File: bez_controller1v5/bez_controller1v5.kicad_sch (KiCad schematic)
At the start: 71 parts, among them J1 Conn_01x03_Male, J10 Barrel_Jack, J11 Conn_01x03_Male, J12 Conn_01x03_Male, J13 USB_B_Mini, J2 Conn_01x03_Male, J3 Conn_01x03_Male, J4 Conn_01x03_Male, J5 Conn_01x03_Male, J6 Conn_01x03_Male, J7 Conn_01x03_Male, J8 IMU Conn_01x08_Female, J9 JTAG Conn_01x06_Male, U1 74LVC2G241, U10 STM32F446RETx, U11 USBLC6-2SC6, U2 74LVC2G241, U3 74LVC2G241, U4 74LVC2G241, U5 74LVC2G241, U6 74LVC2G241, U7 PX07806-500-S, U8 LF50ABV_TO220, U9 LD1117AS33TR_SOT223, Y1 8MHz

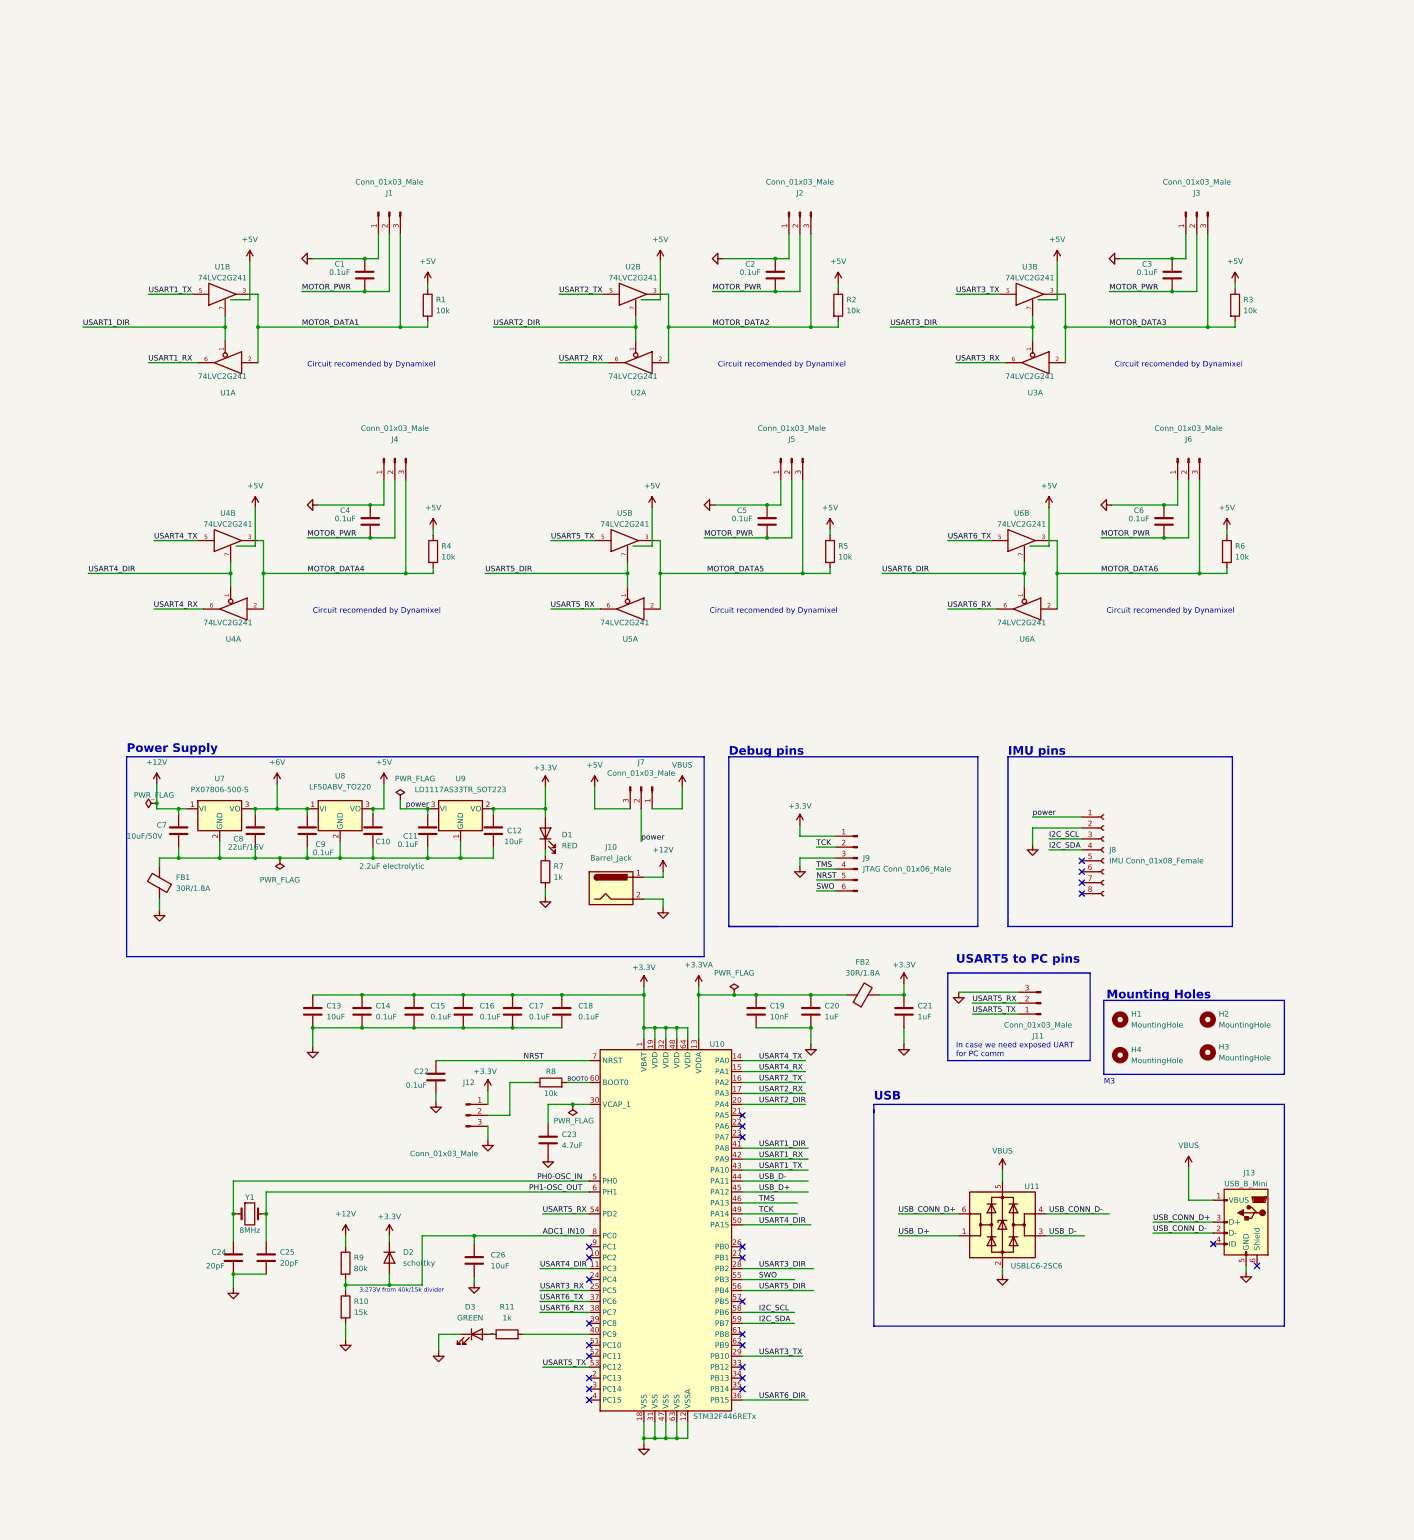
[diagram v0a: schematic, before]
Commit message: uart4 fixed, board cutout, fix layout, signal routing done except for buffers
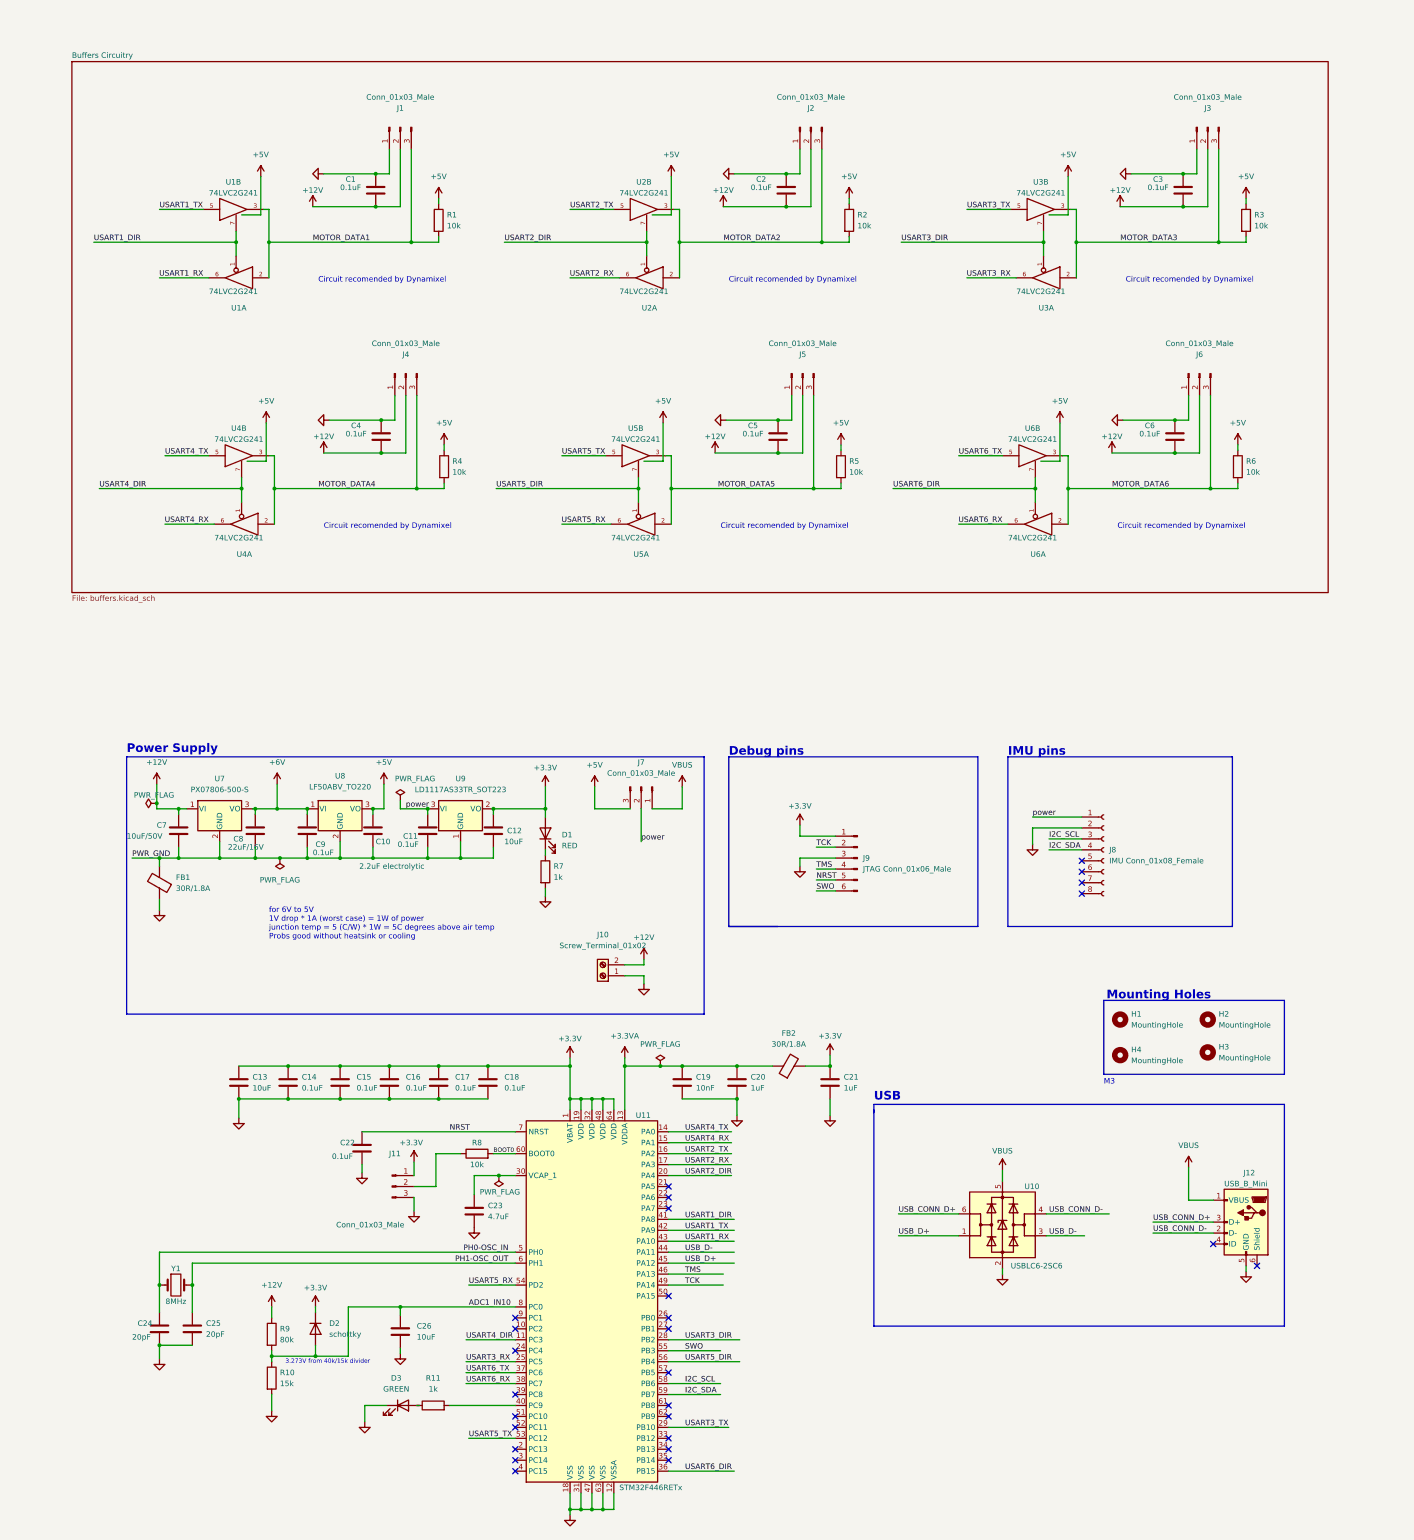
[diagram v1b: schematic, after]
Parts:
- removed J10: Barrel_Jack, Connector_BarrelJack:BarrelJack_Horizontal, symbol Connector:Barrel_Jack
- removed J11: Conn_01x03_Male, Connector_PinHeader_2.54mm:PinHeader_1x03_P2.54mm_Vertical, symbol Connector:Conn_01x03_Male
- added J10: Screw_Terminal_01x02, TerminalBlock:TerminalBlock_bornier-2_P5.08mm, symbol Connector:Screw_Terminal_01x02
- U7: footprint Package_TO_SOT_THT:TO-220-3_Vertical -> Package_TO_SOT_THT:TO-220F-3_Vertical
- U8: footprint Package_TO_SOT_THT:TO-220-3_Horizontal_TabDown -> Package_TO_SOT_THT:TO-220-3_Vertical
- renumbered J12 to J11, J13 to J12, U11 to U10, U10 to U11
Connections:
- net MOTOR_PWR is gone; now on net +12V: C1.2, C2.2, C3.2, C4.2, C5.2, C6.2, J1.2 (Pin_2), J2.2 (Pin_2), J3.2 (Pin_2), J4.2 (Pin_2), J5.2 (Pin_2), J6.2 (Pin_2)
- net +12V: now also J10.2 (Pin_2)
- net GND: now also J10.1 (Pin_1)
- net USART1_RX: now also U11.43 (PA10); no longer U11.42 (PA9)
- net USART1_TX: now also U11.42 (PA9); no longer U11.43 (PA10)
- net USART4_DIR: no longer U11.50 (PA15)
- net PWR_GND: now reaches C10.2, C11.2, C12.2, C7.2, C8.2, C9.2, FB1.2, U7.2 (GND), U8.2 (GND), U9.1 (GND)
- no-connect marks 26 -> 27
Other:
- added sheet Buffers Circuitry (buffers.kicad_sch)
- note added: "for 6V to 5V 1V drop * 1A (worst case) = 1W of power junction temp = 5 (C/W) * 1W = 5C degrees above air temp Probs good without heatsink or cooling"
- note removed: "In case we need exposed UART for PC comm"
- note removed: "USART5 to PC pins"
- moved on the sheet: C1, C13, C14, C15, C16, C17, C18, C19, C2, C20, C21, C22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

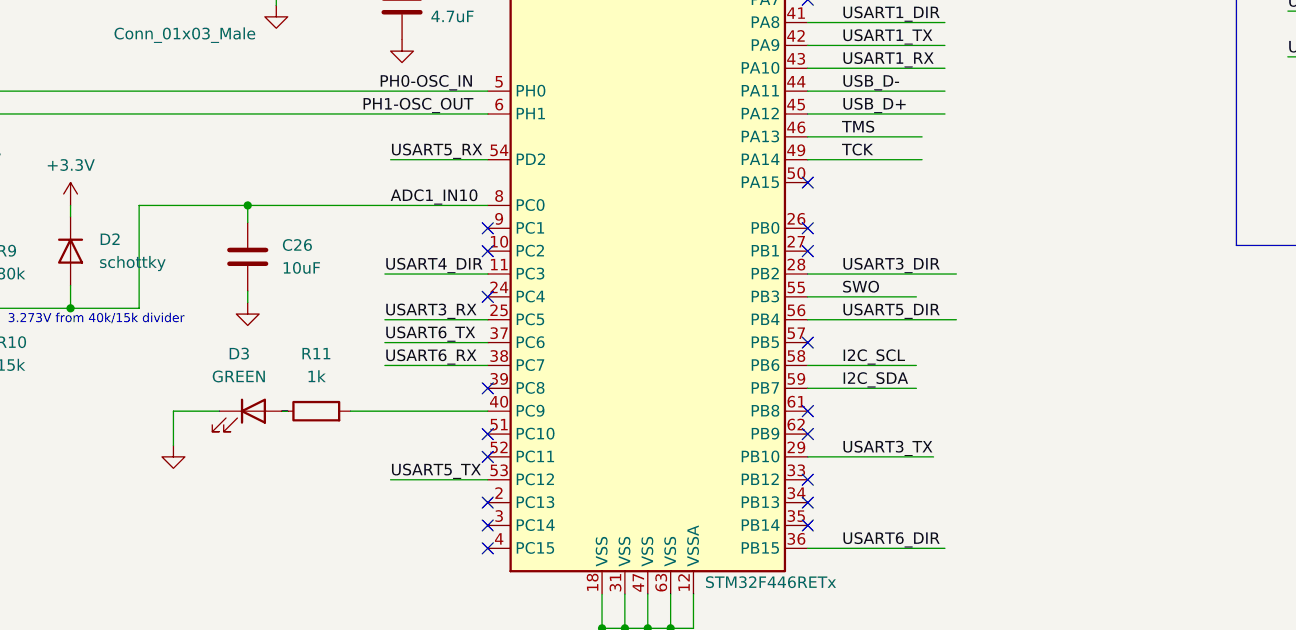
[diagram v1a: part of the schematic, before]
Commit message: finished routing signals
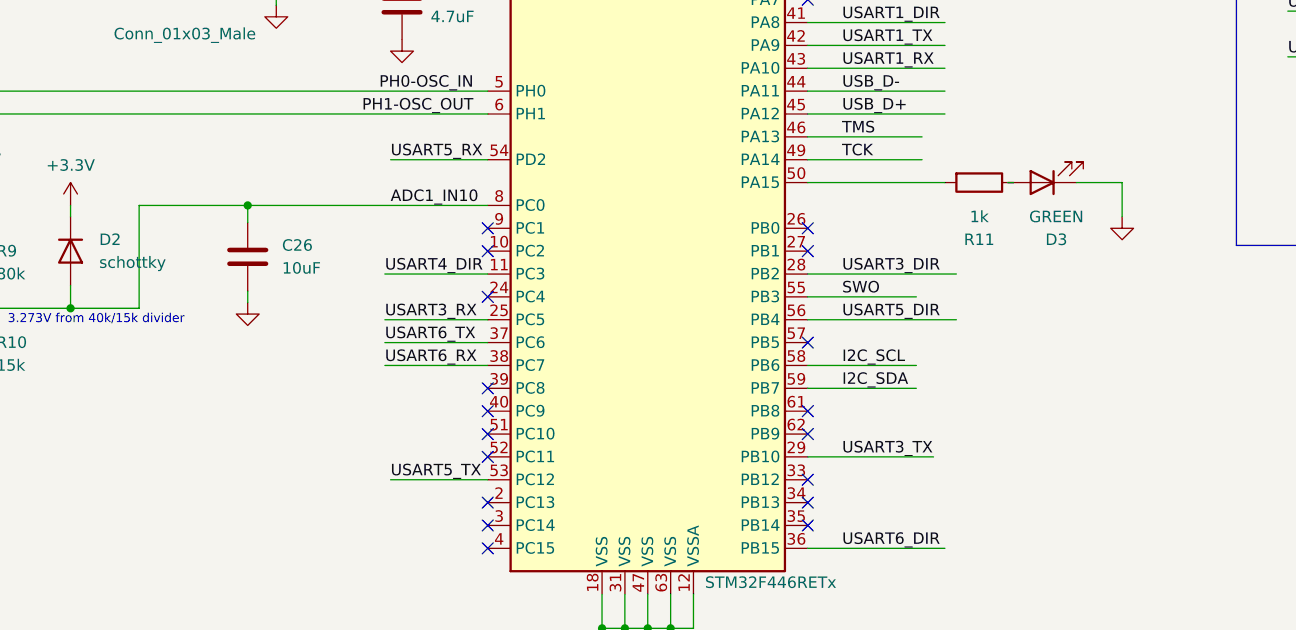
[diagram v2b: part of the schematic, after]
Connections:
- net at R11.2: now also U11.50 (PA15); no longer U11.40 (PC9)
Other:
- moved on the sheet: D3, R11
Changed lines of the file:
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@@
   (no_connect (at 140.335 175.26))
   (no_connect (at 140.335 116.84))
+  (no_connect (at 104.775 167.64))
   (no_connect (at 140.335 160.02))
   (no_connect (at 104.775 180.34))
@@
   (no_connect (at 236.22 41.275))
   (no_connect (at 140.335 147.32))
-  (no_connect (at 140.335 142.24))
   (no_connect (at 104.775 182.88))
   (no_connect (at 140.335 119.38))
@@
     (stroke (width 0) (type default) (color 0 0 0 0))
   )
-  (wire (pts (xy 69.85 167.64) (xy 69.85 171.45))
+  (wire (pts (xy 175.26 142.24) (xy 175.26 146.05))
     (stroke (width 0) (type default) (color 0 0 0 0))
   )
@@
     (stroke (width 0) (type default) (color 0 0 0 0))
   )
-  (wire (pts (xy 74.93 167.64) (xy 69.85 167.64))
+  (wire (pts (xy 170.18 142.24) (xy 175.26 142.24))
     (stroke (width 0) (type default) (color 0 0 0 0))
   )
@@
     (stroke (width 0) (type default) (color 0 0 0 0))
   )
-  (wire (pts (xy 89.535 167.64) (xy 104.775 167.64))
+  (wire (pts (xy 155.575 142.24) (xy 140.335 142.24))
     (stroke (width 0) (type default) (color 0 0 0 0))
   )
@@
     (stroke (width 0) (type default) (color 0 0 0 0))
   )
-  (wire (pts (xy 82.55 167.64) (xy 81.915 167.64))
+  (wire (pts (xy 162.56 142.24) (xy 163.195 142.24))
     (stroke (width 0) (type default) (color 0 0 0 0))
   )
@@
     (pin "1")
   )
-  (symbol (lib_id "Device:R") (at 85.725 167.64 90) (unit 1)
+  (symbol (lib_id "Device:R") (at 159.385 142.24 270) (unit 1)
     (in_bom yes) (on_board yes) (fields_autoplaced)
-    (property "Reference" "R11" (id 0) (at 85.725 161.29 90))
-    (property "Value" "1k" (id 1) (at 85.725 163.83 90))
-    (property "Footprint" "Resistor_THT:R_Axial_DIN0204_L3.6mm_D1.6mm_P5.08mm_Horizontal" (id 2) (at 85.725 169.418 90)
+    (property "Reference" "R11" (id 0) (at 159.385 148.59 90))
+    (property "Value" "1k" (id 1) (at 159.385 146.05 90))
+    (property "Footprint" "Resistor_THT:R_Axial_DIN0204_L3.6mm_D1.6mm_P5.08mm_Horizontal" (id 2) (at 159.385 140.462 90)
       (effects (font (size 1.27 1.27)) hide)
     )
-    (property "Datasheet" "~" (id 3) (at 85.725 167.64 0)
+    (property "Datasheet" "~" (id 3) (at 159.385 142.24 0)
       (effects (font (size 1.27 1.27)) hide)
     )
@@
     (pin "9")
   )
-  (symbol (lib_id "power:GND") (at 69.85 171.45 0) (unit 1)
+  (symbol (lib_id "power:GND") (at 175.26 146.05 0) (unit 1)
     (in_bom yes) (on_board yes) (fields_autoplaced)
-    (property "Reference" "#PWR057" (id 0) (at 69.85 177.8 0)
+    (property "Reference" "#PWR057" (id 0) (at 175.26 152.4 0)
       (effects (font (size 1.27 1.27)) hide)
     )
-    (property "Value" "GND" (id 1) (at 69.85 176.53 0)
+    (property "Value" "GND" (id 1) (at 175.26 151.13 0)
       (effects (font (size 1.27 1.27)) hide)
     )
-    (property "Footprint" "" (id 2) (at 69.85 171.45 0)
+    (property "Footprint" "" (id 2) (at 175.26 146.05 0)
       (effects (font (size 1.27 1.27)) hide)
     )
-    (property "Datasheet" "" (id 3) (at 69.85 171.45 0)
+    (property "Datasheet" "" (id 3) (at 175.26 146.05 0)
       (effects (font (size 1.27 1.27)) hide)
     )
@@
     (pin "1")
   )
-  (symbol (lib_id "Device:LED") (at 78.74 167.64 0) (unit 1)
+  (symbol (lib_id "Device:LED") (at 166.37 142.24 180) (unit 1)
     (in_bom yes) (on_board yes) (fields_autoplaced)
-    (property "Reference" "D3" (id 0) (at 77.1525 161.29 0))
-    (property "Value" "GREEN" (id 1) (at 77.1525 163.83 0))
-    (property "Footprint" "LED_THT:LED_D5.0mm_Clear" (id 2) (at 78.74 167.64 0)
+    (property "Reference" "D3" (id 0) (at 167.9575 148.59 0))
+    (property "Value" "GREEN" (id 1) (at 167.9575 146.05 0))
+    (property "Footprint" "LED_THT:LED_D5.0mm_Clear" (id 2) (at 166.37 142.24 0)
       (effects (font (size 1.27 1.27)) hide)
     )
-    (property "Datasheet" "~" (id 3) (at 78.74 167.64 0)
+    (property "Datasheet" "~" (id 3) (at 166.37 142.24 0)
       (effects (font (size 1.27 1.27)) hide)
     )

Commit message: all signals and power done, need to deal with errors now
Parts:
- removed C26: 10uF, Capacitor_THT:C_Disc_D5.0mm_W2.5mm_P5.00mm, symbol Device:C
- removed D2: schottky, Diode_THT:D_5W_P5.08mm_Vertical_KathodeUp, symbol Device:D
- removed R10: 15k, Resistor_THT:R_Axial_DIN0204_L3.6mm_D1.6mm_P5.08mm_Horizontal, symbol Device:R
- removed R9: 80k, Resistor_THT:R_Axial_DIN0204_L3.6mm_D1.6mm_P5.08mm_Horizontal, symbol Device:R
- C10: footprint Capacitor_THT:C_Disc_D5.0mm_W2.5mm_P5.00mm -> Capacitor_THT:C_Radial_D4.0mm_H7.0mm_P1.50mm
- C12, C13, C7, C8: footprint Capacitor_THT:C_Disc_D5.0mm_W2.5mm_P5.00mm -> Capacitor_THT:C_Radial_D5.0mm_H11.0mm_P2.00mm
- renumbered D3 to D2, R11 to R9
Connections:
- net ADC1_IN10: no longer names the net of U11.8 (PC0)
- no-connect marks 27 -> 28
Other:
- note removed: "3.273V from 40k/15k divider"

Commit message: fixed errors, added labels, custom usb footprint
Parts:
- J12: footprint Connector_USB:USB_Mini-B_Lumberg_2486_01_Horizontal -> Connector_USB:USB_Micro-B_Molex-105017-0001
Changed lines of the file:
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@@
       (effects (font (size 1.27 1.27)) (justify right))
     )
-    (property "Footprint" "Connector_USB:USB_Mini-B_Lumberg_2486_01_Horizontal" (id 2) (at 270.51 126.365 0)
+    (property "Footprint" "Connector_USB:USB_Micro-B_Molex-105017-0001" (id 2) (at 270.51 126.365 0)
       (effects (font (size 1.27 1.27)) hide)
     )
@@
     )
     (path "/7b319a20-c9b9-4bdb-ba6d-e9e1d4356557"
-      (reference "J12") (unit 1) (value "USB_B_Mini") (footprint "Connector_USB:USB_Mini-B_Lumberg_2486_01_Horizontal")
+      (reference "J12") (unit 1) (value "USB_B_Mini") (footprint "Connector_USB:USB_Micro-B_Molex-105017-0001")
     )
     (path "/c6107e00-c08d-48b4-bd93-f1c2a28409df"

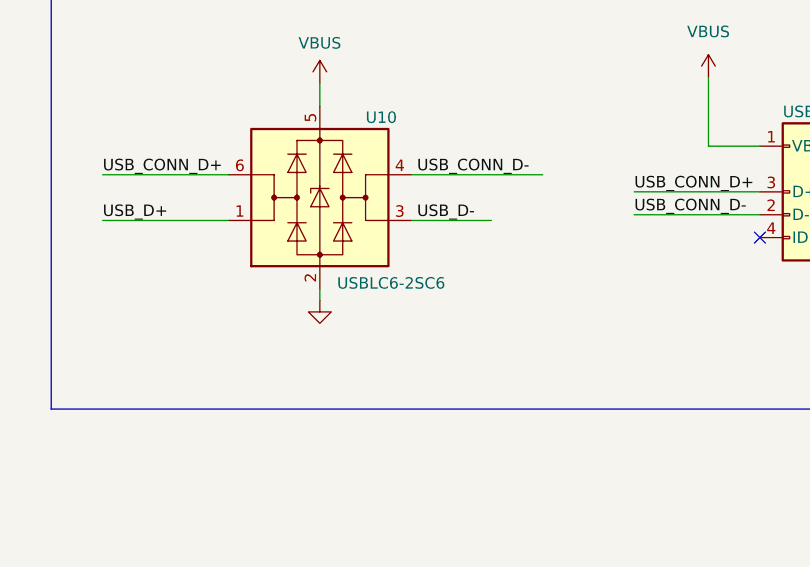
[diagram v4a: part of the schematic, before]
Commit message: selected wrong usb protection
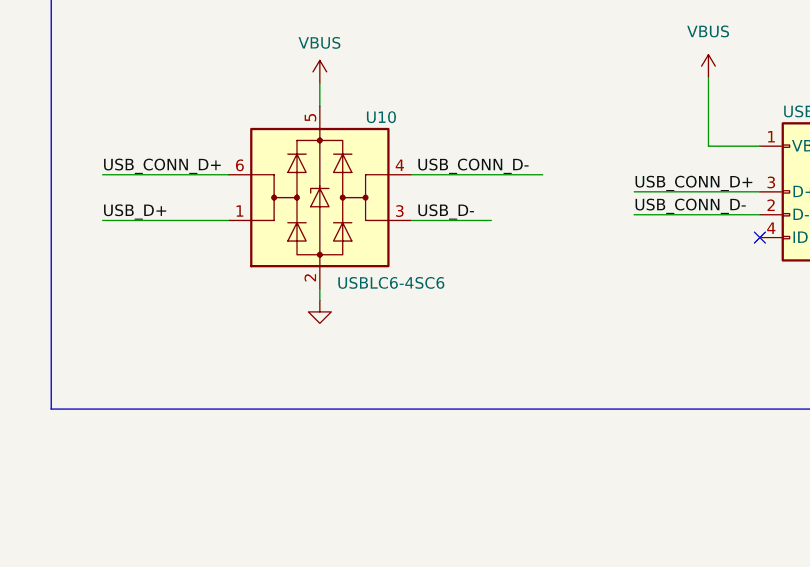
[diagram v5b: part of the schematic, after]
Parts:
- U10: value USBLC6-2SC6 -> USBLC6-4SC6
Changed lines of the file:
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@@
       (effects (font (size 1.27 1.27)) (justify left))
     )
-    (property "Value" "USBLC6-2SC6" (id 1) (at 219.71 135.255 0)
+    (property "Value" "USBLC6-4SC6" (id 1) (at 219.71 135.255 0)
       (effects (font (size 1.27 1.27)) (justify left))
     )
@@
     )
     (path "/a3e60d78-8f0c-489c-bb93-f33bf2d06331"
-      (reference "U10") (unit 1) (value "USBLC6-2SC6") (footprint "Package_TO_SOT_SMD:SOT-23-6")
+      (reference "U10") (unit 1) (value "USBLC6-4SC6") (footprint "Package_TO_SOT_SMD:SOT-23-6")
     )
     (path "/600ad990-a858-4b9c-b042-6f5c64a82f42"
